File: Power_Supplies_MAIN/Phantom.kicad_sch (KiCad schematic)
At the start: 10 parts, among them IC2 LM2940IMPX-10_NOPB, IC3 XC6902NA01PR-G, J11 PINHD_1x4_Female, J12 PINHD_1x8_Female, J8 PINHD_1x3_Female

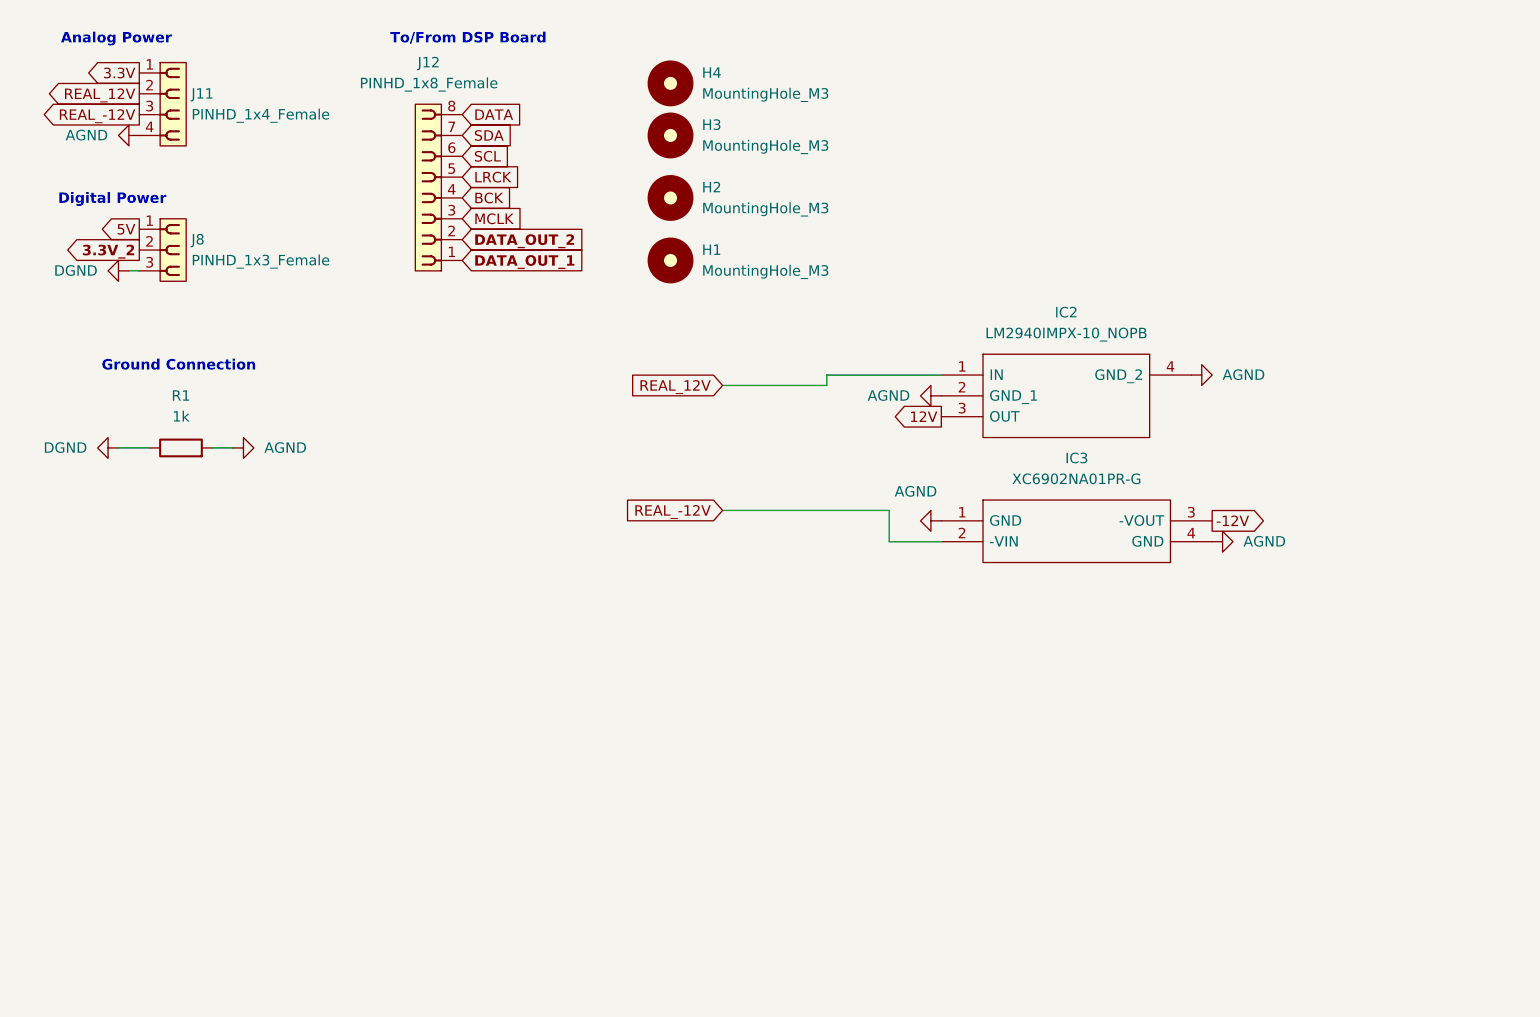
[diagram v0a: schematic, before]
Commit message: updated main PCB to reflect changes w/ new mcu
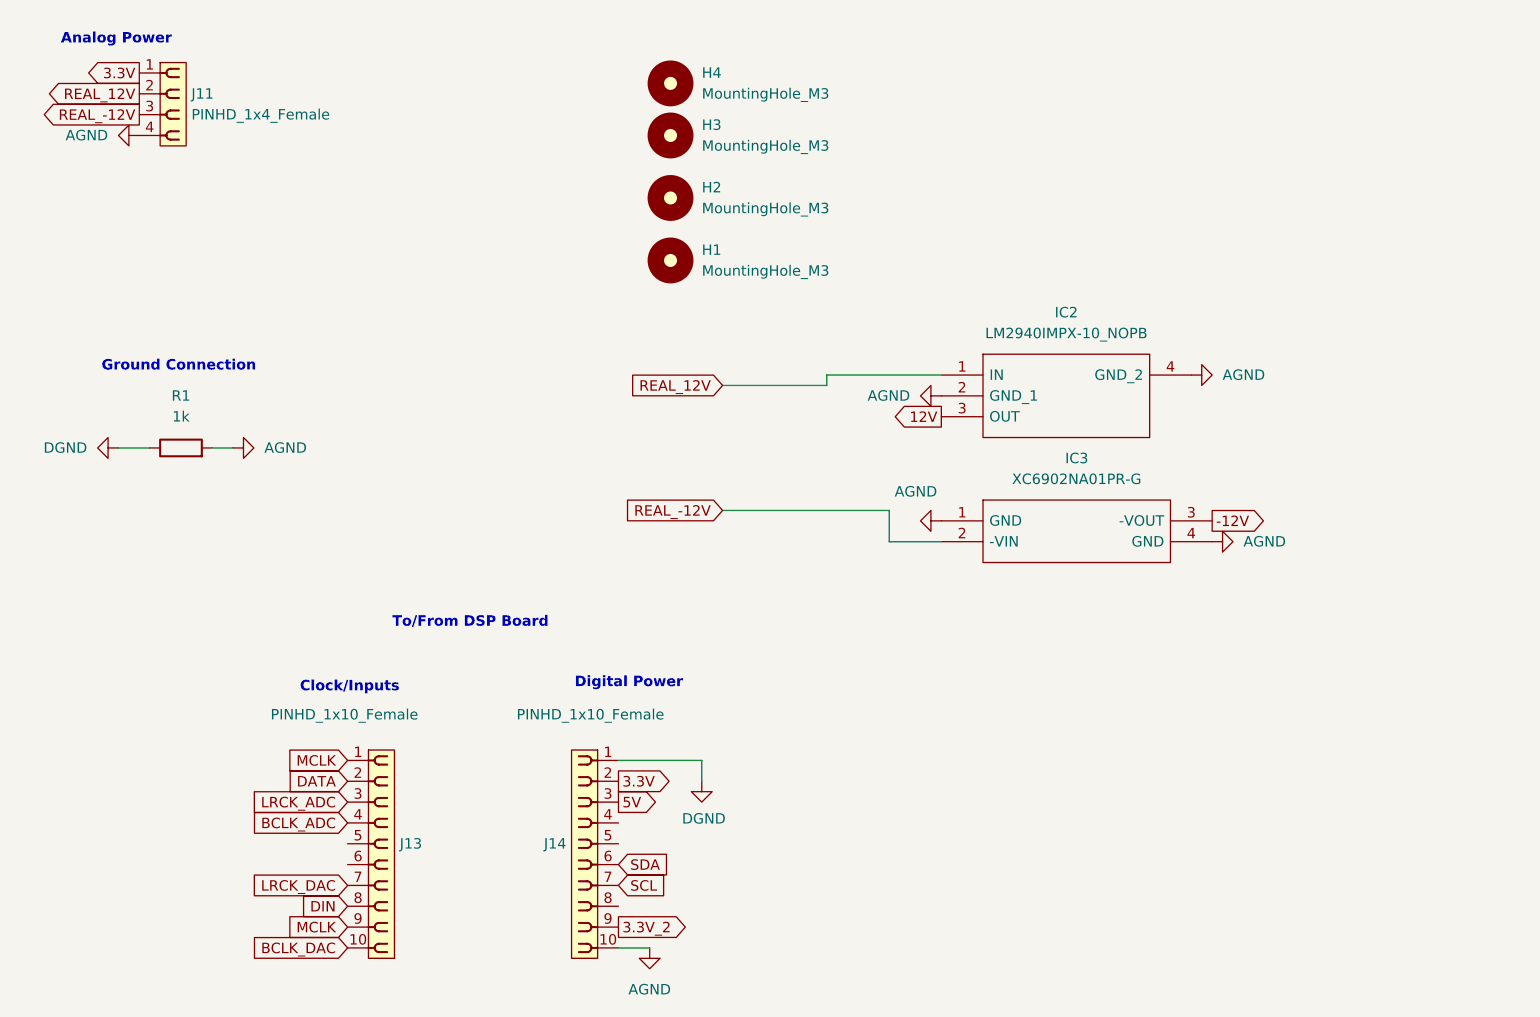
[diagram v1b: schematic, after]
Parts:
- removed J12: PINHD_1x8_Female, Connector_PinSocket_2.54mm:PinSocket_1x08_P2.54mm_Vertical, symbol PCM_SL_Pin_Headers:PINHD_1x8_Female
- removed J8: PINHD_1x3_Female, Connector_PinSocket_2.54mm:PinSocket_1x03_P2.54mm_Vertical, symbol PCM_SL_Pin_Headers:PINHD_1x3_Female
- added J13, J14: PINHD_1x10_Female, Connector_PinSocket_2.54mm:PinSocket_1x10_P2.54mm_Vertical, symbol PCM_SL_Pin_Headers:PINHD_1x10_Female
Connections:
- net 3.3V: now also J14.2
- net 3.3V_2: now also J14.9
- net 5V: now also J14.3
- net AGND: now also J14.10
- net DATA: now also J13.2
- net DGND: now also J14.1
- net MCLK: now also J13.1, J13.9
- net SCL: now also J14.7
- net SDA: now also J14.6
- new net BCLK_ADC: J13.4
- new net BCLK_DAC: J13.10
- new net DIN: J13.8
- new net LRCK_ADC: J13.3
- new net LRCK_DAC: J13.7
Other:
- note added: "Clock/Inputs"

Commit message: added changes that weeks wanted 🐷
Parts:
- added R2, R3: 0R, Resistor_SMD:R_0805_2012Metric_Pad1.20x1.40mm_HandSolder, symbol Device:R
- R1: value 1k -> 0R
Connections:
- net AGND: now also R2.2, R3.2; no longer J14.10
- net DGND: now also R2.1, R3.1

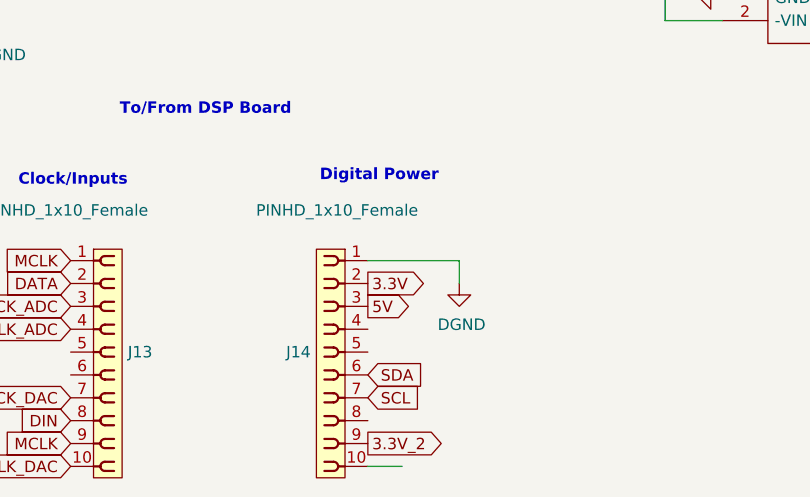
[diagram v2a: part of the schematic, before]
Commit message: fixed issue w mcu getting analog voltage supply (will just use digital)
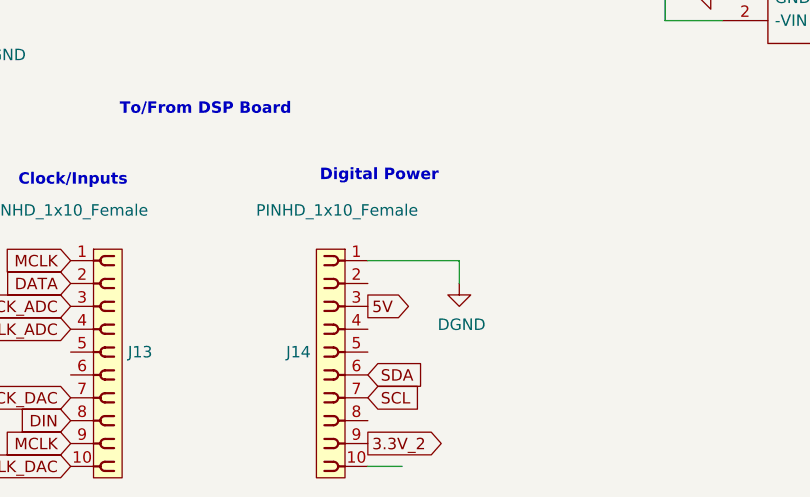
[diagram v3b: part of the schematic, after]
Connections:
- net 3.3V: no longer J14.2
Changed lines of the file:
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@@
-		)
-	)
-	(global_label "3.3V"
-		(shape output)
-		(at 85.09 116.84 0)
-		(fields_autoplaced yes)
-		(effects
-			(font
-				(size 1.27 1.27)
-			)
-			(justify left)
-		)
-		(property "Intersheetrefs" "${INTERSHEET_REFS}"
-			(at 92.1876 116.84 0)
-			(effects
-				(font
-					(size 1.27 1.27)
-				)
-				(justify left)
-				(hide yes)
-			)
 		)
 	)

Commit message: fixed a lot of stuff
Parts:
- removed J11: PINHD_1x4_Female, Connector_PinSocket_2.54mm:PinSocket_1x04_P2.54mm_Vertical, symbol PCM_SL_Pin_Headers:PINHD_1x4_Female
- added C5, C6: 1uF, PCM_Capacitor_SMD_AKL:C_0805_2012Metric, symbol PCM_Capacitor_AKL:C_0805
- added C7: 0.47uF, PCM_Capacitor_SMD_AKL:C_0805_2012Metric, symbol PCM_Capacitor_AKL:C_0805
- added C8: 22uF, Capacitor_SMD:CP_Elec_4x5.8, symbol Device:C_Polarized_US
- added D7, D8: LED, LED_SMD:LED_0402_1005Metric_Pad0.77x0.64mm_HandSolder, symbol PCM_SL_Devices:LED
- added J11: PINHD_1x1_Male, Connector_PinHeader_2.54mm:PinHeader_1x01_P2.54mm_Vertical, symbol PCM_SL_Pin_Headers:PINHD_1x1_Male
- added J16: PINHD_1x5_Male, Connector_PinHeader_2.54mm:PinHeader_1x05_P2.54mm_Vertical, symbol PCM_SL_Pin_Headers:PINHD_1x5_Male
- added J8: PINHD_1x5_Female, Connector_PinSocket_2.54mm:PinSocket_1x05_P2.54mm_Vertical, symbol PCM_SL_Pin_Headers:PINHD_1x5_Female
- added R11, R12, R41, R9: 50, Resistor_SMD:R_0805_2012Metric_Pad1.20x1.40mm_HandSolder, symbol Device:R
- added R15, R16: 2.2k, Resistor_SMD:R_0805_2012Metric, symbol Device:R
- added R36, R42, R8: 0R, Resistor_SMD:R_0805_2012Metric_Pad1.20x1.40mm_HandSolder, symbol Device:R
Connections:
- net -12V: now also C6.1, D7.1
- net 12V: now also C8.1, D8.2
- net 3.3V: now also J16.5, J8.1
- net 3.3V_2: now also J14.3, J11.1
- net 5V: now also J16.2, J8.4; no longer J14.3
- net AGND: now also C5.2, C6.2, C7.2, C8.2, J16.1, J8.5, R15.2, R16.2; no longer IC3.4 (GND)
- net BCLK_ADC: now also R9.1; no longer J13.4
- net BCLK_DAC: now also R42.1; no longer J13.10
- net DATA: now also R36.1; no longer J13.2
- net DIN: now also R12.1; no longer J13.8
- net LRCK_ADC: now also R11.1; no longer J13.3
- net LRCK_DAC: now also R8.1; no longer J13.7
- net MCLK: now also R41.1; no longer J13.9
- net REAL_-12V: now also IC3.4 (GND), C5.1, J16.3, J8.3
- net REAL_12V: now also C7.1, J16.4, J8.2
- new net: J13.9, R41.2
- new net: D8.1, R16.1
- new net: J13.2, R12.2
- new net: D7.2, R15.1
- new net: J13.7, R8.2
- new net: J13.8, R36.2
- new net: J13.10, R42.2
- new net: J13.3, R11.2
- new net: J13.4, R9.2
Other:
- note added: "Connector to get Power to Digital Power Portion"
